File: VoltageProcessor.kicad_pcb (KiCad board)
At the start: 2 copper layers, 25.4 x 100 mm, 29 parts, among them J1 PJ301M-12, J2 PJ301M-12, J3 Eurorack power, J4 PJ301M-12, J5 PJ301M-12, U1 TL074

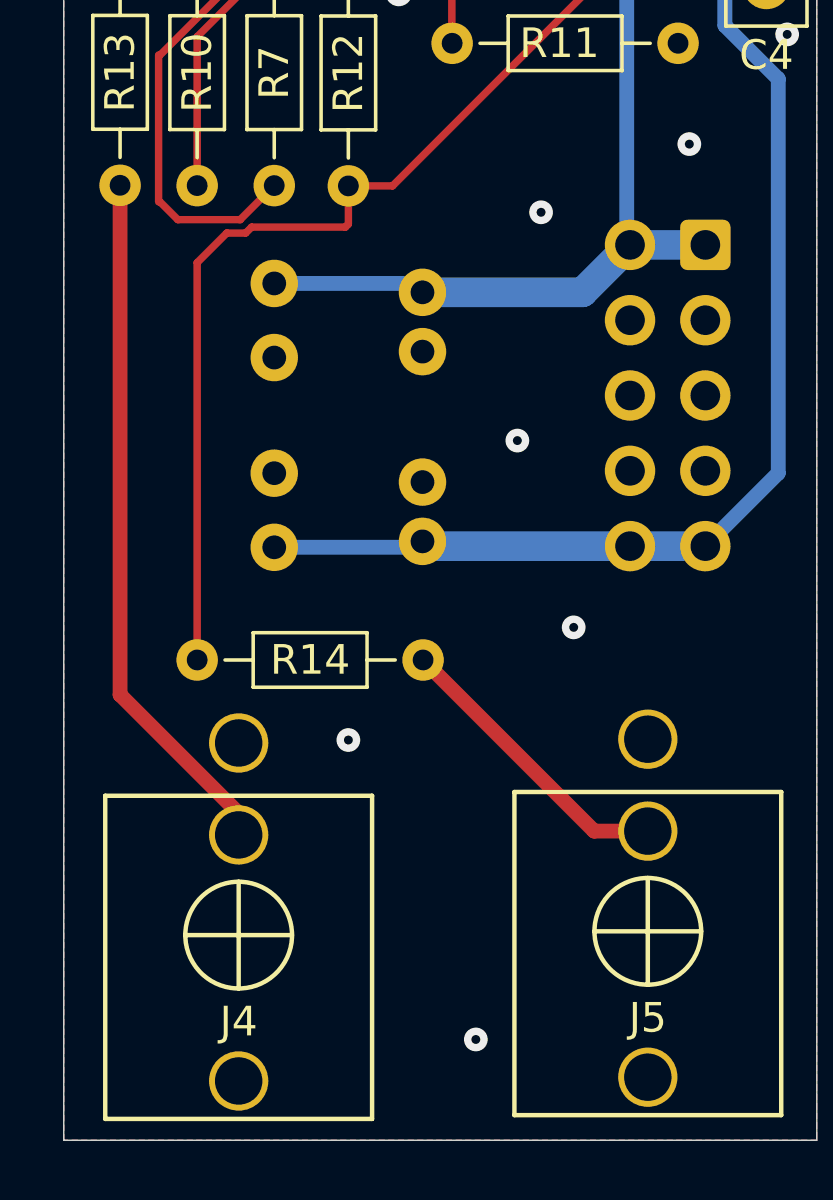
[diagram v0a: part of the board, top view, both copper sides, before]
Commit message: Swapped `U1B` inputs to match that of `U1A`, so that it does work
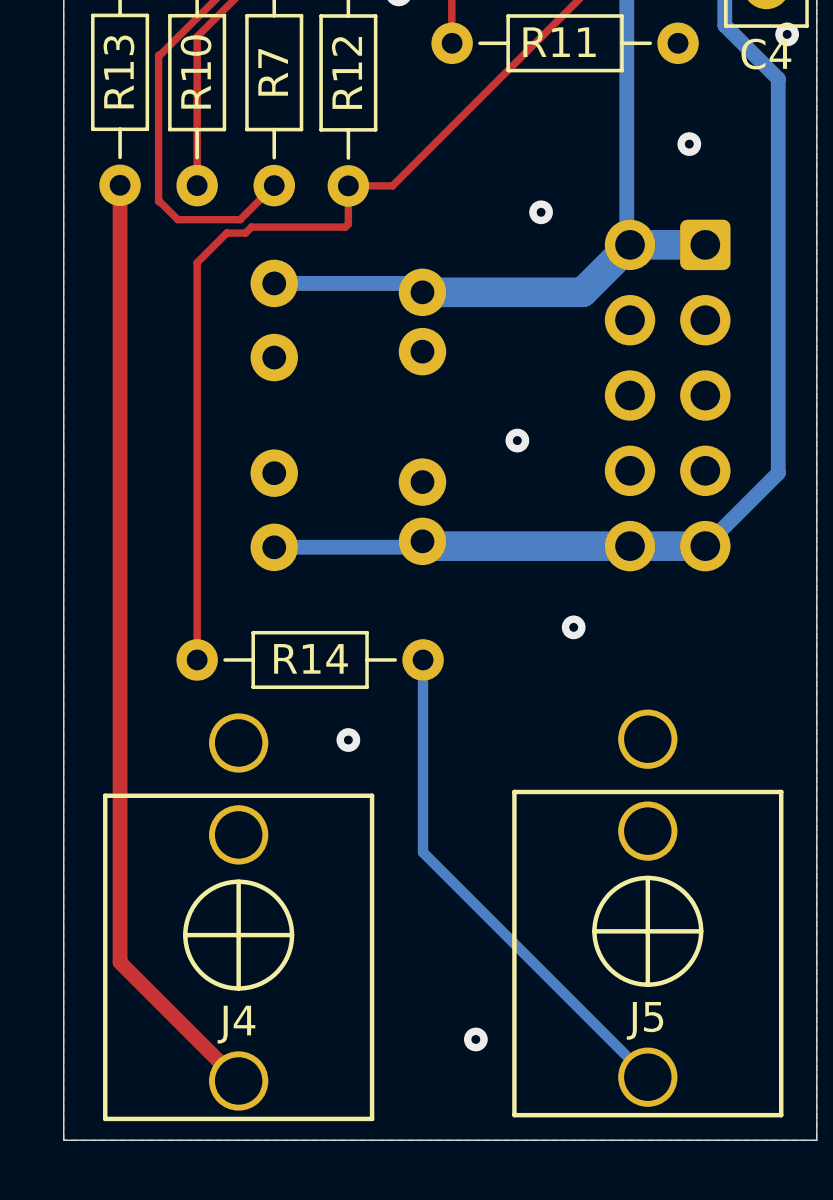
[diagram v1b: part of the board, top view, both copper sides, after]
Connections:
- J4 pad 2: Net-(J4-Pad2) -> unconnected-(J4-Pad2)
- J4 pad 3: unconnected-(J4-Pad3) -> Net-(J4-Pad3)
- J5 pad 2: Net-(J5-Pad2) -> unconnected-(J5-Pad2)
- J5 pad 3: unconnected-(J5-Pad3) -> Net-(J5-Pad3)
- R13 pad 2: Net-(J4-Pad2) -> Net-(J4-Pad3)
- R14 pad 2: Net-(J5-Pad2) -> Net-(J5-Pad3)
- U1 pad 6: unconnected-(U1B---Pad6) -> GND
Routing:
- net Net-(J4-Pad3): track 0.00 -> 31.9 mm
- net Net-(J4-Pad2): track 23.1 -> 0.00 mm
- net Net-(J5-Pad3): track 0.00 -> 17.2 mm
- net Net-(J5-Pad2): track 9.97 -> 0.00 mm
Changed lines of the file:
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@@
 	(net 4 "Net-(J2-Pad3)")
 	(net 5 "Net-(U1A--)")
-	(net 6 "Net-(J4-Pad2)")
+	(net 6 "unconnected-(J4-Pad2)")
 	(net 7 "Net-(U1C--)")
 	(net 8 "Net-(U1B-+)")
-	(net 9 "unconnected-(J4-Pad3)")
+	(net 9 "Net-(J4-Pad3)")
 	(net 10 "Net-(R7-Pad1)")
-	(net 11 "unconnected-(J5-Pad3)")
+	(net 11 "Net-(J5-Pad3)")
 	(net 12 "Net-(U1D--)")
-	(net 13 "Net-(J5-Pad2)")
+	(net 13 "unconnected-(J5-Pad2)")
 	(net 14 "Net-(U1D-+)")
 	(net 15 "Net-(R1-Pad1)")
@@
 	(net 20 "Net-(R10-Pad2)")
 	(net 21 "Net-(R12-Pad2)")
-	(net 22 "unconnected-(U1B---Pad6)")
 	(footprint "Resistor_THT:R_Axial_DIN0204_L3.6mm_D1.6mm_P7.62mm_Horizontal"
 		(layer "F.Cu")
@@
 			(layers "*.Cu" "*.Mask" "F.SilkS")
 			(remove_unused_layers no)
-			(net 6 "Net-(J4-Pad2)")
-			(pintype "passive")
+			(net 6 "unconnected-(J4-Pad2)")
+			(pintype "passive+no_connect")
 		)
 		(pad "3" thru_hole circle
@@
 			(layers "*.Cu" "*.Mask" "F.SilkS")
 			(remove_unused_layers no)
-			(net 9 "unconnected-(J4-Pad3)")
-			(pintype "passive+no_connect")
+			(net 9 "Net-(J4-Pad3)")
+			(pintype "passive")
 		)
 		(model "${USER_LIBRARIES}/AudioJacks/AudioJacks.3dshapes/PJ301M-12_Knurl_nut.step"
@@
 			(layers "*.Cu" "*.Mask")
 			(remove_unused_layers no)
-			(net 13 "Net-(J5-Pad2)")
+			(net 11 "Net-(J5-Pad3)")
 			(pintype "passive")
 		)
@@
 			(layers "*.Cu" "*.Mask" "F.SilkS")
 			(remove_unused_layers no)
-			(net 13 "Net-(J5-Pad2)")
-			(pintype "passive")
+			(net 13 "unconnected-(J5-Pad2)")
+			(pintype "passive+no_connect")
 		)
 		(pad "3" thru_hole circle
@@
 			(layers "*.Cu" "*.Mask" "F.SilkS")
 			(remove_unused_layers no)
-			(net 11 "unconnected-(J5-Pad3)")
-			(pintype "passive+no_connect")
+			(net 11 "Net-(J5-Pad3)")
+			(pintype "passive")
 		)
 		(model "${USER_LIBRARIES}/AudioJacks/AudioJacks.3dshapes/PJ301M-12_Knurl_nut.step"
@@
 			(layers "*.Cu" "*.Mask")
 			(remove_unused_layers no)
-			(net 22 "unconnected-(U1B---Pad6)")
+			(net 2 "GND")
 			(pinfunction "-")
 			(pintype "input")
@@
 			(layers "*.Cu" "*.Mask")
 			(remove_unused_layers no)
-			(net 6 "Net-(J4-Pad2)")
+			(net 9 "Net-(J4-Pad3)")
 			(pintype "passive")
 		)
@@
 	)
 	(segment
-		(start 96.7 124.54)
-		(end 96.7 141.7225)
-		(width 0.5)
-		(layer "F.Cu")
-		(net 6)
-	)
-	(segment
-		(start 96.7 141.7225)
-		(end 100.9 145.9225)
-		(width 0.5)
-		(layer "F.Cu")
-		(net 6)
-	)
-	(segment
 		(start 102.34 112.31)
 		(end 102.34 114.35)
@@
 	)
 	(segment
+		(start 96.7 124.54)
+		(end 96.7 150.75)
+		(width 0.5)
+		(layer "F.Cu")
+		(net 9)
+	)
+	(segment
+		(start 96.7 150.75)
+		(end 100.7 154.75)
+		(width 0.5)
+		(layer "F.Cu")
+		(net 9)
+	)
+	(segment
 		(start 100.75 125.7)
 		(end 101.9 124.55)
@@
 	)
 	(segment
+		(start 106.92 147.0425)
+		(end 114.5 154.6225)
+		(width 0.35)
+		(layer "B.Cu")
+		(net 11)
+	)
+	(segment
+		(start 106.92 140.55)
+		(end 106.92 147.0425)
+		(width 0.35)
+		(layer "B.Cu")
+		(net 11)
+	)
+	(segment
 		(start 112.5 114.35)
 		(end 109.7 117.15)
@@
 	)
 	(segment
-		(start 106.92 140.55)
-		(end 112.6925 146.3225)
-		(width 0.5)
-		(layer "F.Cu")
-		(net 13)
-	)
-	(segment
-		(start 112.6925 146.3225)
-		(end 114.5 146.3225)
-		(width 0.5)
-		(layer "F.Cu")
-		(net 13)
-	)
-	(segment

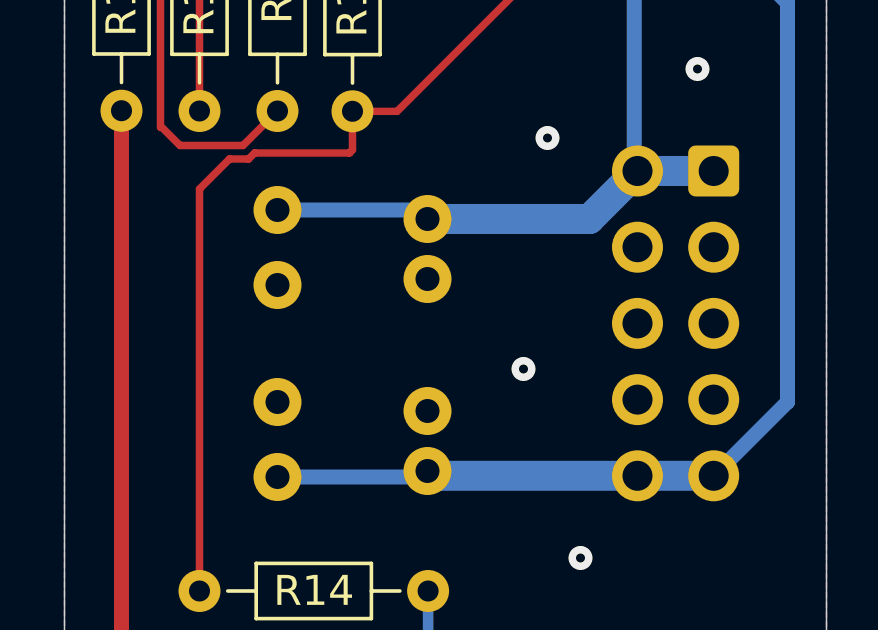
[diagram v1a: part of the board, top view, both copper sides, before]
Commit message: Implemented fixes in schematic
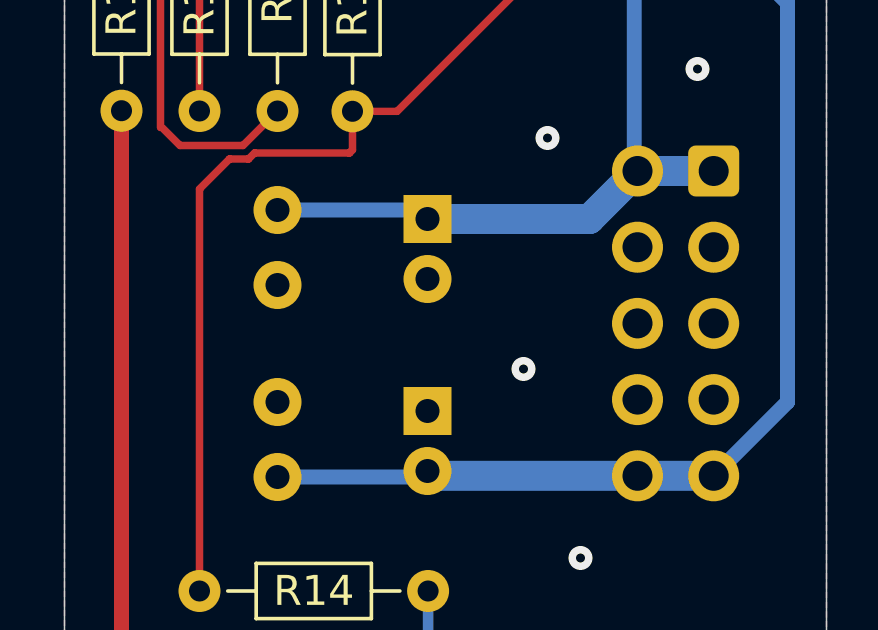
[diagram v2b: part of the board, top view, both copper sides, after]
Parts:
- C5, C6: footprint Capacitor_THT:C_Radial_D5.0mm_H11.0mm_P2.00mm -> Capacitor_THT:CP_Radial_D5.0mm_P2.00mm
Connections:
- J3 pad 1: +12V -> -12V
- J3 pad 10: -12V -> +12V
- J3 pad 2: +12V -> -12V
- J3 pad 9: -12V -> +12V
- R1 pad 2: Net-(U1B-+) -> Net-(U1B--)
- R11 pad 2: Net-(U1D--) -> Net-(U1D-+)
- R12 pad 1: Net-(U1D-+) -> Net-(U1D--)
- R3 pad 1: Net-(U1B-+) -> Net-(U1B--)
- R8 pad 2: Net-(U1D-+) -> Net-(U1D--)
- R9 pad 2: Net-(U1D--) -> Net-(U1D-+)
- RV1 pad 1: Net-(J1-Pad3) -> GND
- RV1 pad 3: GND -> Net-(J1-Pad3)
- RV2 pad 1: Net-(J2-Pad3) -> GND
- RV2 pad 3: GND -> Net-(J2-Pad3)
- U1 pad 5: Net-(U1B-+) -> GND
- U1 pad 6: GND -> Net-(U1B--)
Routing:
- net Net-(U1B-+): track 20.6 -> 0.00 mm
- net GND: track 17.9 -> 38.5 mm

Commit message: Remove all tracks
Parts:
- moved C6 6.35 mm to (106.9, 128.2)
- moved C1 6.35 mm to (101.9, 134.2)
- moved C2 6.35 mm to (101.9, 127.9)
- moved C5 6.35 mm to (106.9, 134.5)
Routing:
- net -12V: track 67.8 -> 0.00 mm
- net +12V: track 66.7 -> 0.00 mm
- net Net-(U1C--): track 41.2 -> 0.00 mm, vias 2 -> 0
- net GND: track 38.5 -> 0.00 mm, vias 21 -> 0
- net Net-(R12-Pad2): track 35.8 -> 0.00 mm
- net Net-(R7-Pad1): track 34.6 -> 0.00 mm, vias 1 -> 0
- net Net-(J4-Pad3): track 31.9 -> 0.00 mm
- net Net-(J2-Pad3): track 28.7 -> 0.00 mm
- net Net-(J1-Pad3): track 28.2 -> 0.00 mm
- net Net-(R4-Pad2): track 24.3 -> 0.00 mm, vias 4 -> 0
- net Net-(U1A--): track 19.7 -> 0.00 mm
- net Net-(J5-Pad3): track 17.2 -> 0.00 mm
- net Net-(U1D-+): track 15.8 -> 0.00 mm, vias 2 -> 0
- net Net-(R3-Pad2): track 12.4 -> 0.00 mm
- net Net-(U1D--): track 8.37 -> 0.00 mm
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- removed copper zone on B.Cu, net GND
- removed copper zone on F.Cu, net GND

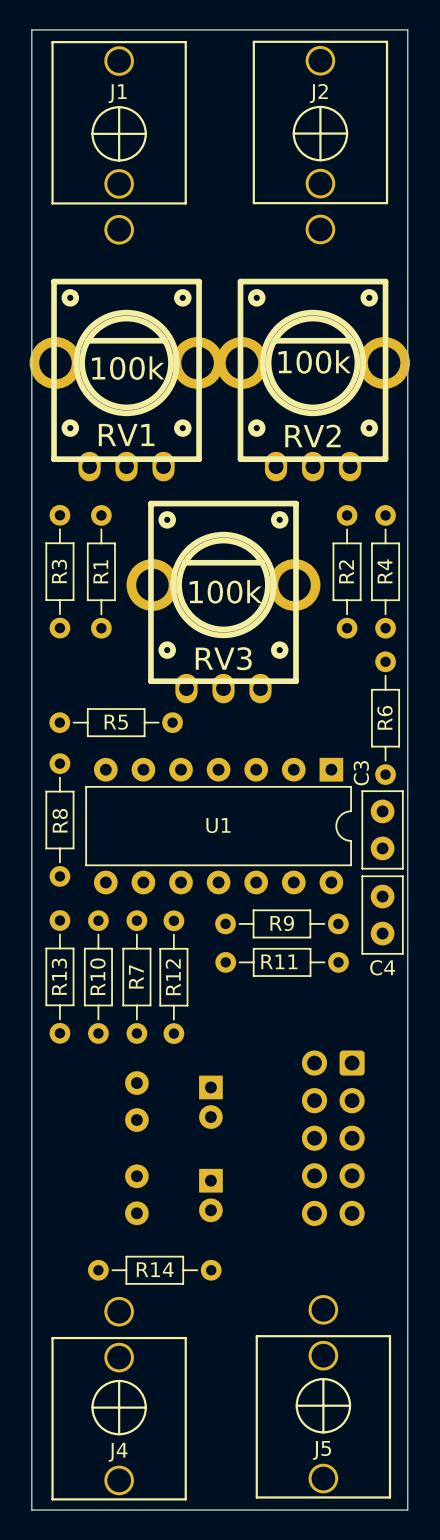
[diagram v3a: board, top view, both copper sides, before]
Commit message: New routing implenting the fixes for rev 0.1
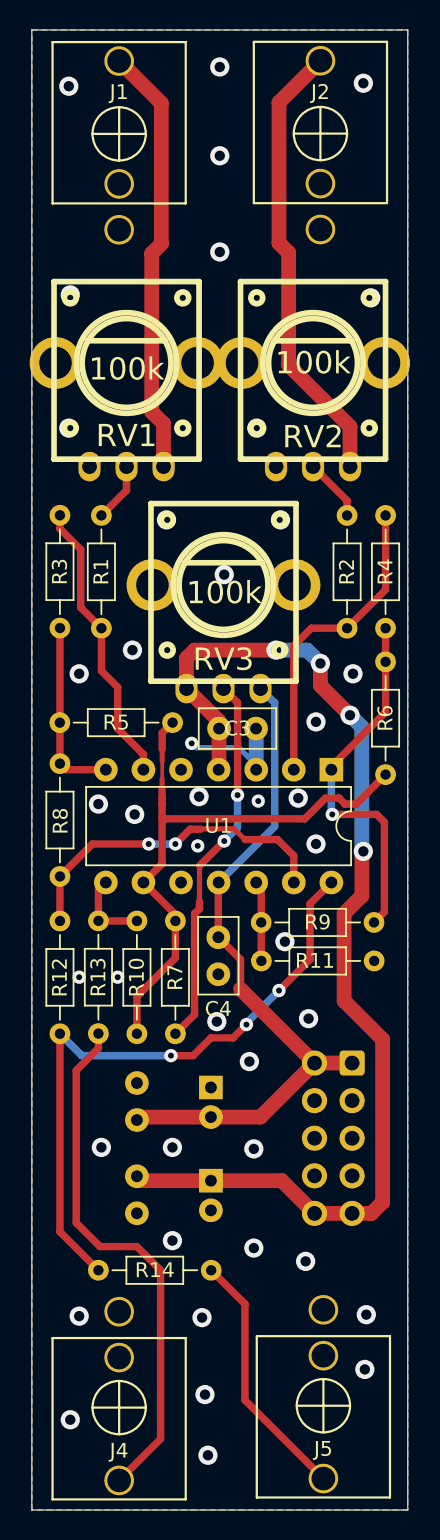
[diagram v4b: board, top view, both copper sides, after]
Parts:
- moved C3 12.4 mm to (107.5, 104.0), turned to 0 degrees
- moved C4 11.4 mm to (107.4, 120.5)
- moved R12 7.70 mm to (96.7, 117.0)
- moved R10 2.60 mm to (101.9, 124.6)
- moved R13 2.60 mm to (99.3, 116.9)
- moved R7 2.60 mm to (104.5, 124.6)
- moved R11 2.41 mm to (117.9, 119.7)
- moved R9 2.41 mm to (117.9, 117.0)
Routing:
- net +12V: track 0.00 -> 75.0 mm, vias 0 -> 4
- net -12V: track 0.00 -> 46.1 mm
- net Net-(R12-Pad2): track 0.00 -> 43.1 mm, vias 0 -> 3
- net Net-(U1C--): track 0.00 -> 40.5 mm
- net Net-(J4-Pad3): track 0.00 -> 35.8 mm
- net Net-(J2-Pad3): track 0.00 -> 30.6 mm
- net Net-(J1-Pad3): track 0.00 -> 29.2 mm
- net Net-(R7-Pad1): track 0.00 -> 25.5 mm, vias 0 -> 2
- net Net-(R4-Pad2): track 0.00 -> 24.9 mm, vias 0 -> 1
- net Net-(U1D--): track 0.00 -> 22.7 mm, vias 0 -> 2
- net Net-(U1A--): track 0.00 -> 21.2 mm
- net Net-(U1B--): track 0.00 -> 19.5 mm
- net Net-(J5-Pad3): track 0.00 -> 17.2 mm
- net Net-(R3-Pad2): track 0.00 -> 12.4 mm
- net GND: track 0.00 -> 8.07 mm, vias 0 -> 43
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- added copper zone on B.Cu, net GND
- added copper zone on F.Cu, net GND
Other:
- board text added: "rev 0.2"
- board text removed: "rev 0.1"

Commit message: Went with old routing instead, with the fixes implemented in the PCB layout. Update README.md
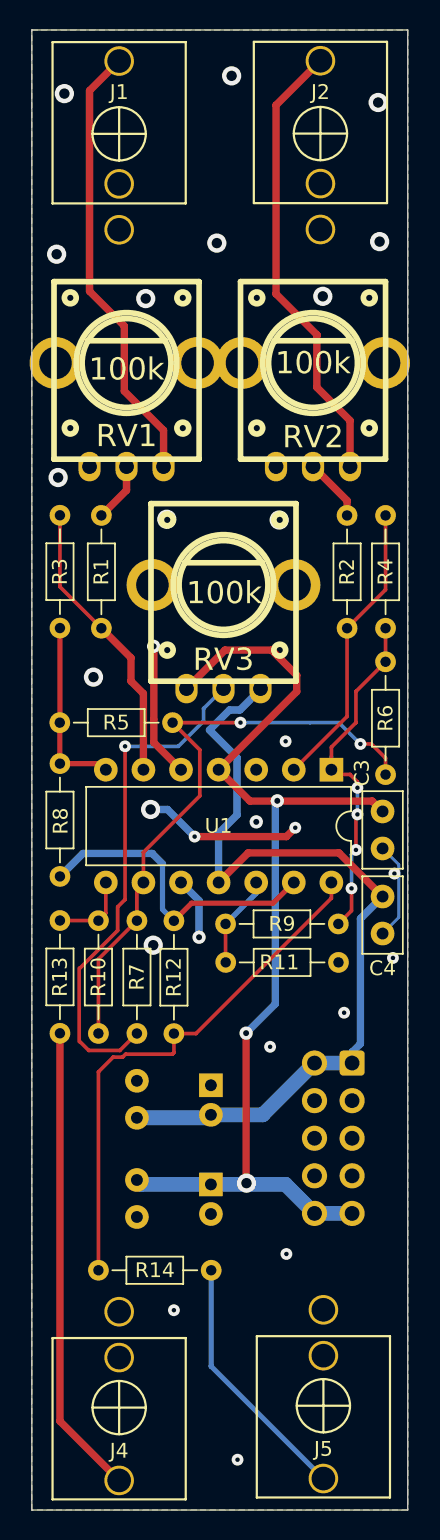
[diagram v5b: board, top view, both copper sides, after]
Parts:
- moved C3 12.4 mm to (118.5, 109.5), turned to -90 degrees
- moved C4 11.4 mm to (118.5, 117.8)
- moved R12 7.70 mm to (104.4, 116.9)
- moved R10 2.60 mm to (99.3, 124.5)
- moved R13 2.60 mm to (96.7, 116.9)
- moved R7 2.60 mm to (101.9, 124.5)
- moved R11 2.41 mm to (115.5, 119.8)
- moved R9 2.41 mm to (115.5, 117.2)
- moved C1 0.25 mm to (101.9, 134.4)
- moved C5 0.25 mm to (106.9, 134.8)
- moved C2 0.15 mm to (101.9, 127.8)
- moved C6 0.15 mm to (106.9, 128.1)
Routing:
- net GND: track 8.07 -> 30.8 mm, vias 43 -> 27
- net -12V: track 46.1 -> 57.7 mm
- net Net-(R7-Pad1): track 25.5 -> 34.6 mm, vias 2 -> 1
- net Net-(R12-Pad2): track 43.1 -> 35.8 mm, vias 3 -> 0
- net Net-(J4-Pad3): track 35.8 -> 31.9 mm
- net +12V: track 75.0 -> 73.1 mm, vias 4 -> 3
- net Net-(U1D--): track 22.7 -> 21.2 mm, vias 2 -> 0
- net Net-(U1A--): track 21.2 -> 19.7 mm
- net Net-(J1-Pad3): track 29.2 -> 30.3 mm
- net Net-(U1D-+): track 5.44 -> 6.26 mm
- net Net-(U1C--): track 40.5 -> 41.2 mm, vias 0 -> 2
- net Net-(R4-Pad2): track 24.9 -> 24.3 mm, vias 1 -> 4
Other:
- board text added: "rev 0.1"
- board text removed: "rev 0.2"

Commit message: Add `R15` `R16` to DC Offset potmeter its range is now `+-10` instead of the `rail-rail` voltage. Add small changes in routing to accomodate the resistors. Add change text to `rev 0.3`
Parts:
- added R15: 10k, Resistor_THT:R_Axial_DIN0204_L3.6mm_D1.6mm_P7.62mm_Horizontal, F.Cu at (111.4, 72.2)
- added R16: 10k, Resistor_THT:R_Axial_DIN0204_L3.6mm_D1.6mm_P7.62mm_Horizontal, F.Cu at (103.7, 69.8)
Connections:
- RV3 pad 1: +12V -> Net-(R15-Pad2)
- RV3 pad 3: -12V -> Net-(R16-Pad1)
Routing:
- net -12V: track 57.7 -> 103.9 mm, vias 0 -> 1
- net Net-(R16-Pad1): track 0.00 -> 37.3 mm
- net Net-(R15-Pad2): track 0.00 -> 33.8 mm
- net +12V: track 73.1 -> 91.6 mm
- net Net-(R7-Pad1): track 34.6 -> 36.1 mm
- net GND: track 30.8 -> 31.6 mm, vias 27 -> 44
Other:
- board text added: "rev 0.3"
- board text removed: "rev 0.1"
